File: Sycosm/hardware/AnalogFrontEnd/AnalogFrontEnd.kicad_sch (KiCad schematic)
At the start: 15 parts, among them J1 Input_6.35mm_TS, J2 Thru_6.35mm_TS, J3 LINEIN_L_6.35mm_TRS, U1 MCP6021-E/SN

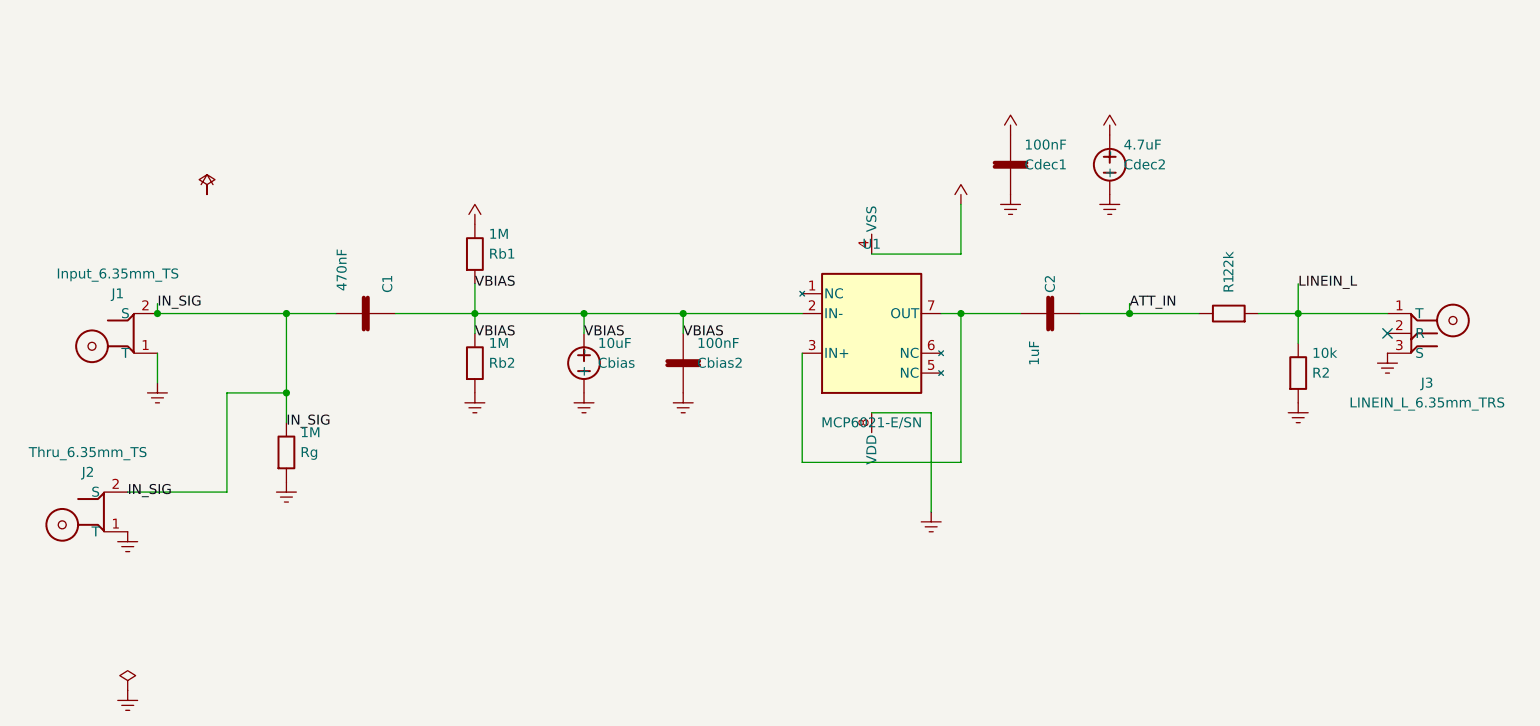
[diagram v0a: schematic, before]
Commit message: feat(hw,afe): update values and opamp pinout, add docs
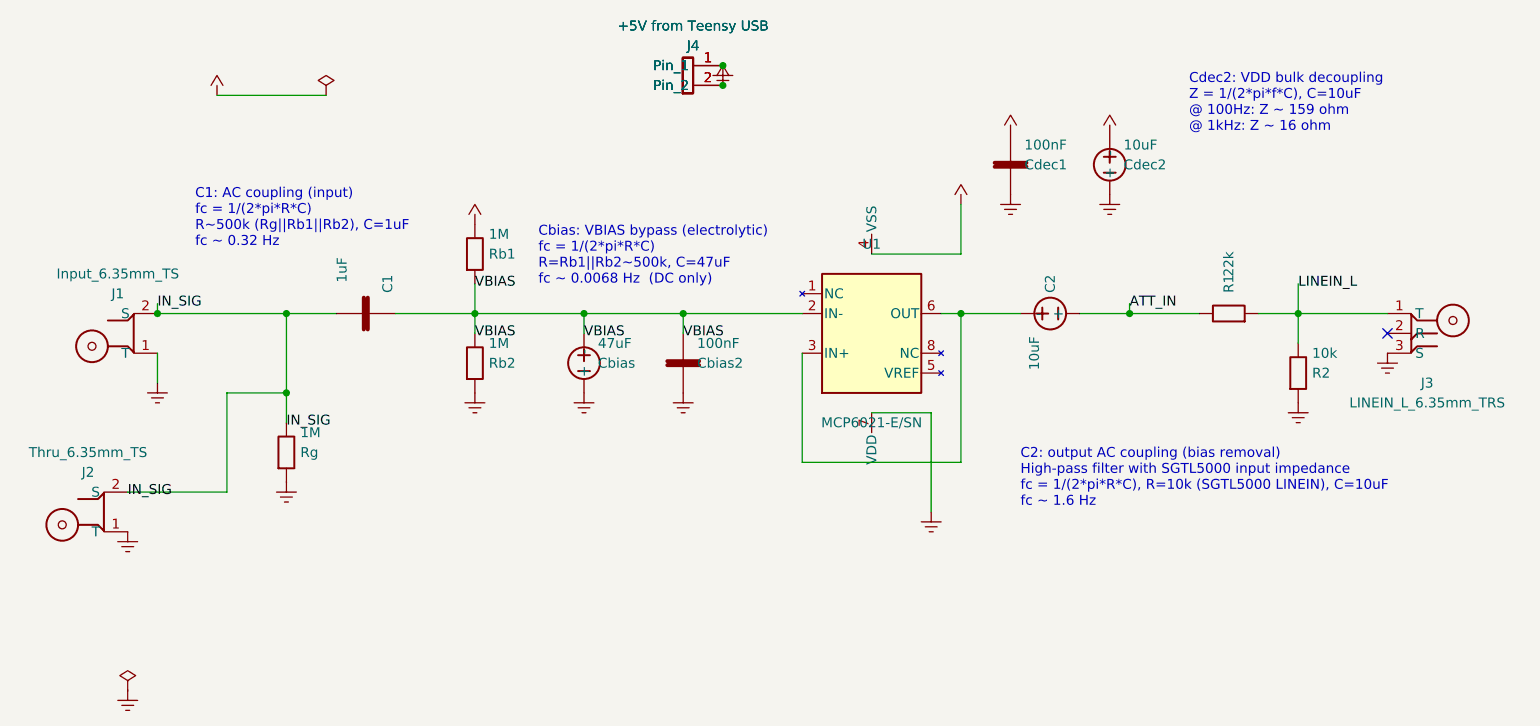
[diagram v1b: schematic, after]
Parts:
- added J4 (x2): +5V from Teensy USB, Connector_PinHeader_2.54mm:PinHeader_1x02_P2.54mm_Vertical, symbol Connector:Conn_01x02
- C1: value 470nF -> 1uF
- C2: value 1uF -> 10uF; symbol Device:C -> Device:CP
- Cbias: value 10uF -> 47uF
- Cdec2: value 4.7uF -> 10uF
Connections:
- net ATT_IN: now also C2.1 (+); no longer C2.2
- net at U1.6 (OUT): now also C2.2 (-), U1.3 (IN+)
- new net: J4.1 (Pin_1), J4.1 (Pin_1)
- new net: J4.2 (Pin_2), J4.2 (Pin_2)
- now unconnected: U1.7 (OUT)
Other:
- note added: "C1: AC coupling (input) fc = 1/(2*pi*R*C) R~500k (Rg||Rb1||Rb2), C=1uF fc ~ 0.32 Hz"
- note added: "C2: output AC coupling (bias removal) High-pass filter with SGTL5000 input impedance fc = 1/(2*pi*R*C), R=10k (SGTL5000 LINEIN), C=10uF fc ~ 1.6 Hz"
- note added: "Cbias: VBIAS bypass (electrolytic) fc = 1/(2*pi*R*C) R=Rb1||Rb2~500k, C=47uF fc ~ 0.0068 Hz (DC only)"
- note added: "Cdec2: VDD bulk decoupling Z = 1/(2*pi*f*C), C=10uF @ 100Hz: Z ~ 159 ohm @ 1kHz: Z ~ 16 ohm"

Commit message: fix: switch + and - in the Opamp, add hw todos
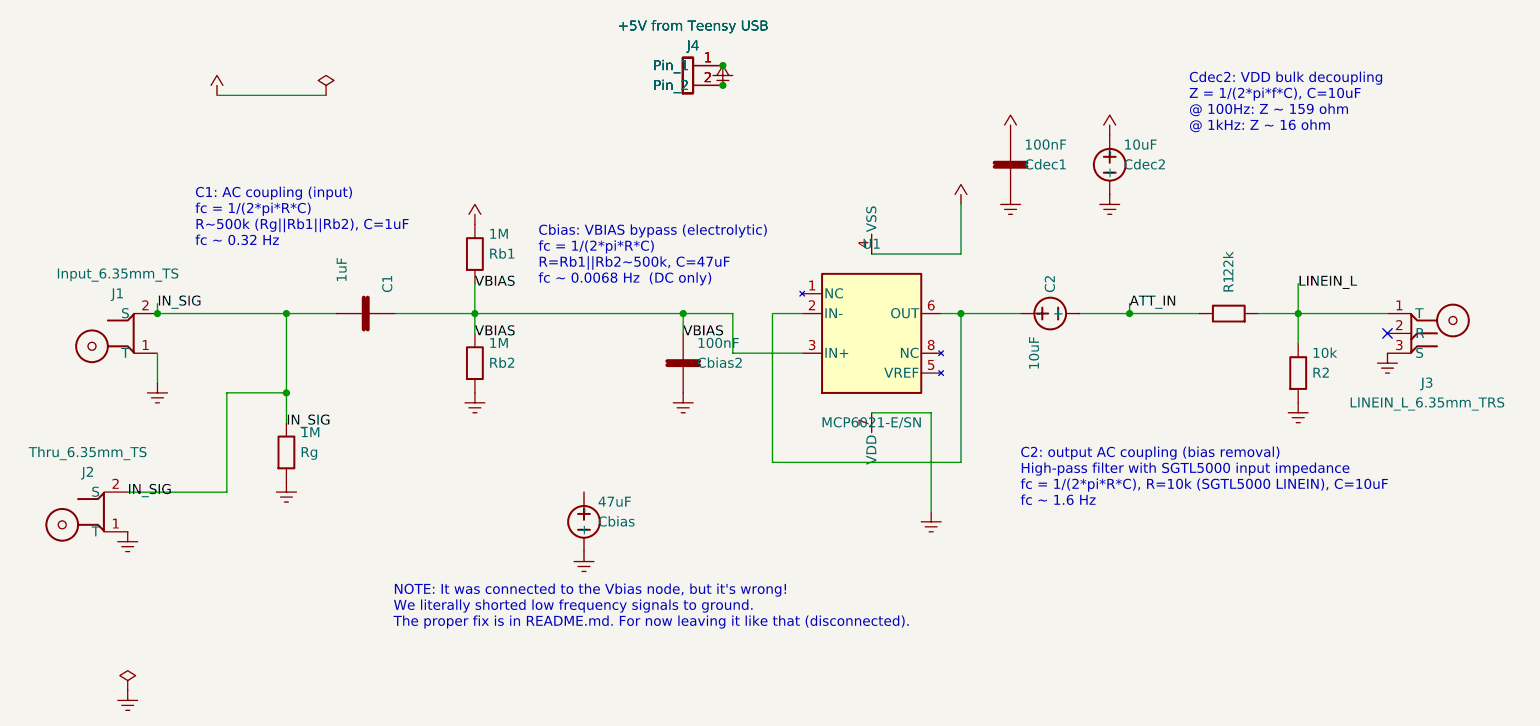
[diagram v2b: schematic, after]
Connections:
- net VBIAS: now also U1.3 (IN+); no longer Cbias.2 (-), U1.2 (IN-)
- net at C2.2 (-), U1.6 (OUT): now also U1.2 (IN-); no longer U1.3 (IN+)
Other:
- note added: "NOTE: It was connected to the Vbias node, but it's wrong! We literally shorted low frequency signals to ground. The proper fix is in README.md. For now leaving it like that (disconnected)."
- moved on the sheet: Cbias
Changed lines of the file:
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@@
+		)
+	)
+	(text "NOTE: It was connected to the Vbias node, but it's wrong!\nWe literally shorted low frequency signals to ground.\nThe proper fix is in README.md. For now leaving it like that (disconnected)."
+		(exclude_from_sim no)
+		(at 64.516 108.712 0)
+		(effects
+			(font
+				(size 1.27 1.27)
+			)
+			(justify left)
 		)
 	)
@@
 	)
 	(junction
+		(at 101.6 71.12)
+		(diameter 0)
+		(color 0 0 0 0)
+	)
+	(junction
 		(at 180.34 71.12)
 		(diameter 0)
@@
 	)
 	(junction
-		(at 101.6 71.12)
-		(diameter 0)
-		(color 0 0 0 0)
-	)
-	(junction
 		(at 106.68 39.37)
 		(diameter 0)
@@
 		(color 0 0 0 0)
 	)
-	(junction
-		(at 88.9 71.12)
-		(diameter 0)
-		(color 0 0 0 0)
-	)
 	(no_connect
 		(at 191.77 73.66)
@@
 	(wire
 		(pts
+			(xy 113.03 90.17) (xy 137.16 90.17)
+		)
+		(stroke
+			(width 0)
+			(type default)
+		)
+	)
+	(wire
+		(pts
 			(xy 50.8 71.12) (xy 57.15 71.12)
 		)
@@
 	(wire
 		(pts
+			(xy 107.95 76.2) (xy 107.95 71.12)
+		)
+		(stroke
+			(width 0)
+			(type default)
+		)
+	)
+	(wire
+		(pts
 			(xy 137.16 57.15) (xy 137.16 63.5)
 		)
@@
 	(wire
 		(pts
-			(xy 116.84 76.2) (xy 116.84 90.17)
-		)
-		(stroke
-			(width 0)
-			(type default)
-		)
-	)
-	(wire
-		(pts
-			(xy 88.9 71.12) (xy 101.6 71.12)
-		)
-		(stroke
-			(width 0)
-			(type default)
-		)
-	)
-	(wire
-		(pts
-			(xy 88.9 71.12) (xy 88.9 73.66)
+			(xy 116.84 71.12) (xy 113.03 71.12)
+		)
+		(stroke
+			(width 0)
+			(type default)
+		)
+	)
+	(wire
+		(pts
+			(xy 116.84 76.2) (xy 107.95 76.2)
 		)
 		(stroke
@@
 	(wire
 		(pts
+			(xy 113.03 71.12) (xy 113.03 90.17)
+		)
+		(stroke
+			(width 0)
+			(type default)
+		)
+	)
+	(wire
+		(pts
 			(xy 175.26 71.12) (xy 180.34 71.12)
 		)
@@
 	(wire
 		(pts
-			(xy 116.84 90.17) (xy 137.16 90.17)
-		)
-		(stroke
-			(width 0)
-			(type default)
-		)
-	)
-	(wire
-		(pts
-			(xy 74.93 71.12) (xy 88.9 71.12)
+			(xy 74.93 71.12) (xy 101.6 71.12)
+		)
+		(stroke
+			(width 0)
+			(type default)
+		)
+	)
+	(wire
+		(pts
+			(xy 107.95 71.12) (xy 101.6 71.12)
 		)
 		(stroke
@@
 		(pts
 			(xy 137.16 71.12) (xy 144.78 71.12)
-		)
-		(stroke
-			(width 0)
-			(type default)
-		)
-	)
-	(wire
-		(pts
-			(xy 101.6 71.12) (xy 116.84 71.12)
 		)
 		(stroke
@@
 	)
 	(label "VBIAS"
-		(at 88.9 73.66 0)
-		(effects
-			(font
-				(size 1.27 1.27)
-			)
-			(justify left)
-		)
-	)
-	(label "VBIAS"
 		(at 74.93 67.31 0)
 		(effects
@@
 	(symbol
 		(lib_id "power:GND")
-		(at 88.9 81.28 0)
+		(at 88.9 101.6 0)
 		(unit 1)
 		(body_style 1)
@@
 		(dnp no)
 		(property "Reference" "#PWR06"
-			(at 88.9 83.82 0)
+			(at 88.9 104.14 0)
 			(hide yes)
 			(show_name no)
@@
 		)
 		(property "Value" "GND"
-			(at 88.9 82.55 0)
+			(at 88.9 102.87 0)
 			(hide yes)
 			(show_name no)
@@
 		)
 		(property "Footprint" ""
-			(at -55.88 -19.05 0)
+			(at -55.88 1.27 0)
 			(hide yes)
 			(show_name no)
@@
 		)
 		(property "Datasheet" ""
-			(at -55.88 -19.05 0)
-			(hide yes)
-			(show_name no)
-			(do_not_autoplace no)
-			(effects
-				(font
-					(size 1.27 1.27)
-				)
-			)
-		)
-		(property "Description" ""
-			(at 88.9 81.28 0)
+			(at -55.88 1.27 0)
+			(hide yes)
+			(show_name no)
+			(do_not_autoplace no)
+			(effects
+				(font
+					(size 1.27 1.27)
+				)
+			)
+		)
+		(property "Description" ""
+			(at 88.9 101.6 0)
 			(show_name no)
 			(do_not_autoplace no)
@@
 	(symbol
 		(lib_id "Device:CP")
-		(at 88.9 77.47 0)
+		(at 88.9 97.79 0)
 		(unit 1)
 		(body_style 1)
@@
 		(dnp no)
 		(property "Reference" "Cbias"
-			(at 90.678 77.47 0)
+			(at 90.678 97.79 0)
 			(show_name no)
 			(do_not_autoplace no)
@@
 		)
 		(property "Value" "47uF"
-			(at 90.678 74.93 0)
+			(at 90.678 95.25 0)
 			(show_name no)
 			(do_not_autoplace no)
@@
 		)
 		(property "Footprint" "Capacitor_SMD:CP_Elec_5x5.8"
-			(at -55.88 -19.05 0)
+			(at -55.88 1.27 0)
 			(hide yes)
 			(show_name no)
@@
 		)
 		(property "Datasheet" "~"
-			(at -55.88 -19.05 0)
-			(hide yes)
-			(show_name no)
-			(do_not_autoplace no)
-			(effects
-				(font
-					(size 1.27 1.27)
-				)
-			)
-		)
-		(property "Description" ""
-			(at 88.9 77.47 0)
-			(show_name no)
-			(do_not_autoplace no)
+			(at -55.88 1.27 0)
+			(hide yes)
+			(show_name no)
+			(do_not_autoplace no)
+			(effects
+				(font
+					(size 1.27 1.27)
+				)
+			)
+		)
+		(property "Description" ""
+			(at 88.9 97.79 0)
+			(show_name no)
+			(do_not_autoplace no)
